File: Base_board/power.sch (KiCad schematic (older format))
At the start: 39 parts, among them J13 Wire pad, J14 Wire pad, J15 Wire pad, J16 Wire pad, J9 USB_A, Q6 2N7002, SW3 SW_Push, U3 MCP16331T-E/CH, U4 BTS50080-1TEA, U5 DC_DC_POL

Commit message: Fix older symbols assignation
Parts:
- C10, C26, C4, C5, C7, C8, C9: symbol KXKM_audio_battery_module-rescue:C_Small -> Device:C_Small
- C6: symbol KXKM_audio_battery_module-rescue:CP1_Small -> Device:CP1_Small
- D13, D2: symbol KXKM_audio_battery_module-rescue:D_Zener_Small -> Device:D_Zener_Small
- D3: symbol KXKM_audio_battery_module-rescue:D_Schottky_Small -> Device:D_Schottky_Small
- L1: symbol KXKM_audio_battery_module-rescue:L_Small -> Device:L_Small
- R1, R10, R12, R22, R8, R9: symbol KXKM_audio_battery_module-rescue:R_Small -> Device:R_Small
- SW3: symbol KXKM_audio_battery_module-rescue:SW_Push -> Switch:SW_Push
- U3: symbol KXKM_audio_battery_module-rescue:MCP16301H -> Regulator_Switching:MCP16331CH
- U5: symbol KXKM_audio_battery_module-rescue:DC_DC_POL -> tom_kicad:DC_DC_POL
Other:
- moved on the sheet: U3
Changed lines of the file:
@@
 EESchema Schematic File Version 4
-LIBS:KXKM_audio_battery_module-cache
+LIBS:KXKM_ESP32_battery_management_board-cache
 EELAYER 29 0
 EELAYER END
@@
 Battery power output.\nMax 10A
 $Comp
-L KXKM_audio_battery_module-rescue:DC_DC_POL U5
+L tom_kicad:DC_DC_POL U5
 U 1 1 5A9FAEA4
 P 8650 2350
@@
 Optional 3A  buck module \nwith USB connector
 $Comp
-L KXKM_audio_battery_module-rescue:SW_Push SW3
+L Switch:SW_Push SW3
 U 1 1 5A9FC5E1
 P 3150 4900
@@
 $EndComp
 $Comp
-L KXKM_audio_battery_module-rescue:GND #PWR035
+L power:GND #PWR035
 U 1 1 5A9FC90F
 P 2150 1700
@@
 MAIN_OUT_EN
 $Comp
-L KXKM_audio_battery_module-rescue:C_Small C5
+L Device:C_Small C5
 U 1 1 5A9FED2B
 P 2000 6800
@@
 $EndComp
 $Comp
-L KXKM_audio_battery_module-rescue:C_Small C4
+L Device:C_Small C4
 U 1 1 5A9FEE3B
 P 1600 6800
@@
 $EndComp
 $Comp
-L KXKM_audio_battery_module-rescue:+BATT #PWR037
+L power:+BATT #PWR037
 U 1 1 5A9FF065
 P 2800 1250
@@
 $EndComp
 $Comp
-L KXKM_audio_battery_module-rescue:GND #PWR038
+L power:GND #PWR038
 U 1 1 5A9FF120
 P 1600 6900
@@
 $EndComp
 $Comp
-L KXKM_audio_battery_module-rescue:GND #PWR039
+L power:GND #PWR039
 U 1 1 5A9FF156
 P 2000 6900
@@
 $EndComp
 $Comp
-L KXKM_audio_battery_module-rescue:C_Small C7
+L Device:C_Small C7
 U 1 1 5A9FF342
 P 3800 6600
@@
 $EndComp
 $Comp
-L KXKM_audio_battery_module-rescue:D_Schottky_Small D3
+L Device:D_Schottky_Small D3
 U 1 1 5A9FF573
 P 3800 6850
@@
 $EndComp
 $Comp
-L KXKM_audio_battery_module-rescue:GND #PWR040
+L power:GND #PWR040
 U 1 1 5A9FF8A5
-P 3250 7350
-F 0 "#PWR040" H 3250 7100 50  0001 C CNN
-F 1 "GND" H 3250 7200 50  0000 C CNN
-F 2 "" H 3250 7350 50  0001 C CNN
-F 3 "" H 3250 7350 50  0001 C CNN
-	1    3250 7350
-	1    0    0    -1
-$EndComp
-$Comp
-L KXKM_audio_battery_module-rescue:GND #PWR041
+P 3250 7050
+F 0 "#PWR040" H 3250 6800 50  0001 C CNN
+F 1 "GND" H 3250 6900 50  0000 C CNN
+F 2 "" H 3250 7050 50  0001 C CNN
+F 3 "" H 3250 7050 50  0001 C CNN
+	1    3250 7050
+	1    0    0    -1
+$EndComp
+$Comp
+L power:GND #PWR041
 U 1 1 5A9FF8DA
 P 3800 6950
@@
 $EndComp
 $Comp
-L KXKM_audio_battery_module-rescue:MCP16301H U3
+L Regulator_Switching:MCP16331CH U3
 U 1 1 5A9FC3B6
-P 3250 6950
-F 0 "U3" H 2950 7500 50  0000 L CNN
-F 1 "MCP16331T-E/CH" H 2950 7400 50  0000 L CNN
-F 2 "Package_TO_SOT_SMD:SOT-23-6" H 3250 6450 50  0001 C CNN
-F 3 "" H 2950 7500 50  0001 C CNN
-	1    3250 6950
-	1    0    0    -1
-$EndComp
-$Comp
-L KXKM_audio_battery_module-rescue:L_Small L1
+P 3250 6750
+F 0 "U3" H 3200 7100 50  0000 L CNN
+F 1 "MCP16331T-E/CH" H 2900 7000 50  0000 L CNN
+F 2 "Package_TO_SOT_SMD:SOT-23-6" H 3250 6250 50  0001 C CNN
+F 3 "" H 2950 7300 50  0001 C CNN
+	1    3250 6750
+	1    0    0    -1
+$EndComp
+$Comp
+L Device:L_Small L1
 U 1 1 5A9FFE27
 P 4300 6750
@@
 $EndComp
 $Comp
-L KXKM_audio_battery_module-rescue:R_Small R9
+L Device:R_Small R9
 U 1 1 5AA004D5
 P 4600 6950
@@
 $EndComp
 $Comp
-L KXKM_audio_battery_module-rescue:R_Small R10
+L Device:R_Small R10
 U 1 1 5AA0053D
 P 4600 7300
@@
 $EndComp
 $Comp
-L KXKM_audio_battery_module-rescue:GND #PWR042
+L power:GND #PWR042
 U 1 1 5AA00713
 P 4600 7450
@@
 $EndComp
 $Comp
-L KXKM_audio_battery_module-rescue:C_Small C8
+L Device:C_Small C8
 U 1 1 5AA00938
 P 5100 6950
@@
 $EndComp
 $Comp
-L KXKM_audio_battery_module-rescue:C_Small C9
+L Device:C_Small C9
 U 1 1 5AA00C46
 P 5500 6950
@@
 $EndComp
 $Comp
-L KXKM_audio_battery_module-rescue:C_Small C10
+L Device:C_Small C10
 U 1 1 5AA00D4C
 P 5950 6950
@@
 $EndComp
 $Comp
-L KXKM_audio_battery_module-rescue:GND #PWR043
+L power:GND #PWR043
 U 1 1 5AA00DA9
 P 5500 7050
@@
 $EndComp
 $Comp
-L KXKM_audio_battery_module-rescue:GND #PWR044
+L power:GND #PWR044
 U 1 1 5AA00DF3
 P 5950 7050
@@
 $EndComp
 $Comp
-L KXKM_audio_battery_module-rescue:+3.3V #PWR045
+L power:+3.3V #PWR045
 U 1 1 5AA00ECC
 P 5950 6700
@@
 3.3V_EN
 $Comp
-L KXKM_audio_battery_module-rescue:D_Zener_Small D2
+L Device:D_Zener_Small D2
 U 1 1 5AA028CA
 P 3150 5600
@@
 $EndComp
 $Comp
-L KXKM_audio_battery_module-rescue:R_Small R8
+L Device:R_Small R8
 U 1 1 5AA0358A
 P 3150 5250
@@
 $EndComp
 $Comp
-L KXKM_audio_battery_module-rescue:GND #PWR047
+L power:GND #PWR047
 U 1 1 5AA037A6
 P 3150 5700
@@
 The MCP16331 has an internal pull up on the EN pin.\n\nOn startup, R1 pulls EN low (system Off)\n\nWhen the push button is pressed, the Zener is powered and \nthe EN pin gets high through D1 => system On.\n\nThe uC gets powered and can now controls the system state \nwith the 3.3V_EN line.\nIt can also monitor future states of the push button.
 $Comp
-L KXKM_audio_battery_module-rescue:VBUS #PWR048
+L power:VBUS #PWR048
 U 1 1 5AA2DF17
 P 9400 2200
@@
 $EndComp
 $Comp
-L KXKM_audio_battery_module-rescue:CP1_Small C6
+L Device:CP1_Small C6
 U 1 1 5AA2FD90
 P 2150 1500
@@
 $EndComp
 $Comp
-L KXKM_audio_battery_module-rescue:GND #PWR051
+L power:GND #PWR051
 U 1 1 5AA32CAF
 P 9400 1650
@@
 $EndComp
 $Comp
-L KXKM_audio_battery_module-rescue:GND #PWR052
+L power:GND #PWR052
 U 1 1 5AA32D09
 P 9400 2600
@@
 10A high side load switch
 $Comp
-L KXKM_audio_battery_module-rescue:GND #PWR053
+L power:GND #PWR053
 U 1 1 5AA356E4
 P 5150 1800
@@
 $EndComp
 $Comp
-L KXKM_audio_battery_module-rescue:GND #PWR054
+L power:GND #PWR054
 U 1 1 5AA35B5B
 P 4800 1800
@@
 $EndComp
 $Comp
-L KXKM_audio_battery_module-rescue:R_Small R12
+L Device:R_Small R12
 U 1 1 5AA35ECE
 P 6800 2150
@@
 $EndComp
 $Comp
-L KXKM_audio_battery_module-rescue:GND #PWR055
+L power:GND #PWR055
 U 1 1 5AA35FB7
 P 6800 2500
@@
 LOAD_I_SENSE
 $Comp
-L KXKM_audio_battery_module-rescue:PWR_FLAG #FLG057
+L power:PWR_FLAG #FLG057
 U 1 1 5AA444FE
 P 6300 6700
@@
 R8 selection :\nZener current : 5mA min, 100mA max \n470R : \n    5mA with VBat = 5.5V\n    57mA with VBat = 30V
 $Comp
-L KXKM_audio_battery_module-rescue:+VSW #PWR062
+L power:+VSW #PWR062
 U 1 1 5AA7A913
 P 7900 1300
@@
 	2000 6650 2000 6700
 Wire Wire Line
-	3650 6950 3700 6950
-Wire Wire Line
-	3700 6950 3700 7150
-Wire Wire Line
 	3700 7150 4600 7150
 Wire Wire Line
@@
 	9300 2400 9400 2400
 $Comp
-L KXKM_audio_battery_module-rescue:R_Small R1
+L Device:R_Small R1
 U 1 1 5AAAA24E
 P 2500 6950
@@
 $EndComp
 $Comp
-L KXKM_audio_battery_module-rescue:GND #PWR063
+L power:GND #PWR063
 U 1 1 5AAAA2EA
 P 2500 7050
@@
 	2800 1350 2800 1400
 $Comp
-L KXKM_audio_battery_module-rescue:GND #PWR0101
+L power:GND #PWR0101
 U 1 1 5C6E6168
 P 2800 1700
@@
 Connection ~ 2800 1350
 $Comp
-L KXKM_audio_battery_module-rescue:C_Small C26
+L Device:C_Small C26
 U 1 1 5C712B7A
 P 2650 6950
@@
 $EndComp
 $Comp
-L KXKM_audio_battery_module-rescue:GND #PWR0106
+L power:GND #PWR0106
 U 1 1 5C717150
 P 2650 7050
@@
 R_IS selection : I_IS = 6mA max\nIn normal conditions, I_IS = I_load / 10000\n=> with R_IS = 2k, I_load = 10A gives 2V. \nThe Zener clamps voltage to 3V (error conditions => I_IS = 5.2mA)
 $Comp
-L KXKM_audio_battery_module-rescue:D_Zener_Small D13
+L Device:D_Zener_Small D13
 U 1 1 5C7A51DB
 P 7050 2150
@@
 	7050 1900 7100 1900
 $Comp
-L KXKM_audio_battery_module-rescue:GND #PWR0107
+L power:GND #PWR0107
 U 1 1 5C7A9F58
 P 7050 2250
@@
 $EndComp
 $Comp
-L KXKM_audio_battery_module-rescue:R_Small R22
+L Device:R_Small R22
 U 1 1 5C7B3CFC
 P 6800 2350
@@
 $EndComp
 $Comp
-L KXKM_audio_battery_module-rescue:GND #PWR0102
+L power:GND #PWR0102
 U 1 1 5C7F26AF
 P 9800 4400
@@
 $EndComp
 $Comp
-L KXKM_audio_battery_module-rescue:GND #PWR0105
+L power:GND #PWR0105
 U 1 1 5C7F2704
 P 9900 4400
@@
 	1900 1650 2150 1650
 $Comp
-L KXKM_audio_battery_module-rescue:+BATT #PWR046
+L power:+BATT #PWR046
 U 1 1 5AA027F2
 P 3150 4600
@@
 	6200 900  6350 900
 $Comp
-L KXKM_audio_battery_module-rescue:+BATT #PWR0108
+L power:+BATT #PWR0108
 U 1 1 5CD9FDB2
 P 1600 6600
@@
 	2150 950  2100 950
 $Comp
-L KXKM_audio_battery_module-rescue:PWR_FLAG #FLG0101
+L power:PWR_FLAG #FLG0101
 U 1 1 5CDEEF8F
 P 2150 900
@@
 	5950 1500 5950 1900
 $Comp
-L KXKM_audio_battery_module-rescue:+BATT #PWR061
+L power:+BATT #PWR061
 U 1 1 5AA46EC2
 P 10350 6200
@@
 $EndComp
 $Comp
-L KXKM_audio_battery_module-rescue:PWR_FLAG #FLG060
+L power:PWR_FLAG #FLG060
 U 1 1 5AA46E7F
 P 10350 6200
@@
 For most newer devices, a 0R resistor between D+ and D-\nshould be enough to indicate that the port can supply up to 1.5A.\n\nOlder Apple devices may need specific voltage dividers \non D+/D- lines.\nCheck https://lygte-info.dk/info/USBinfo%20UK.html
 $Comp
-L KXKM_audio_battery_module-rescue:VBUS #PWR027
+L power:VBUS #PWR027
 U 1 1 5CBCF1C7
 P 9400 3700
@@
 $EndComp
 $Comp
-L KXKM_audio_battery_module-rescue:VBUS #PWR025
+L power:VBUS #PWR025
 U 1 1 5CBD526E
 P 8850 3650
@@
 $EndComp
 $Comp
-L KXKM_audio_battery_module-rescue:VBUS #PWR023
+L power:VBUS #PWR023
 U 1 1 5CBD54F6
 P 8500 3650
@@
 $EndComp
 $Comp
-L KXKM_audio_battery_module-rescue:GND #PWR026
+L power:GND #PWR026
 U 1 1 5CBD5908
 P 8850 4450
@@
 $EndComp
 $Comp
-L KXKM_audio_battery_module-rescue:GND #PWR024
+L power:GND #PWR024
 U 1 1 5CBD5C75
 P 8500 4450
@@
 	9400 4100 9400 4200
 Connection ~ 9300 4200
+Wire Wire Line
+	3650 6850 3700 6850
+Wire Wire Line
+	3700 6850 3700 7150
 $EndSCHEMATC

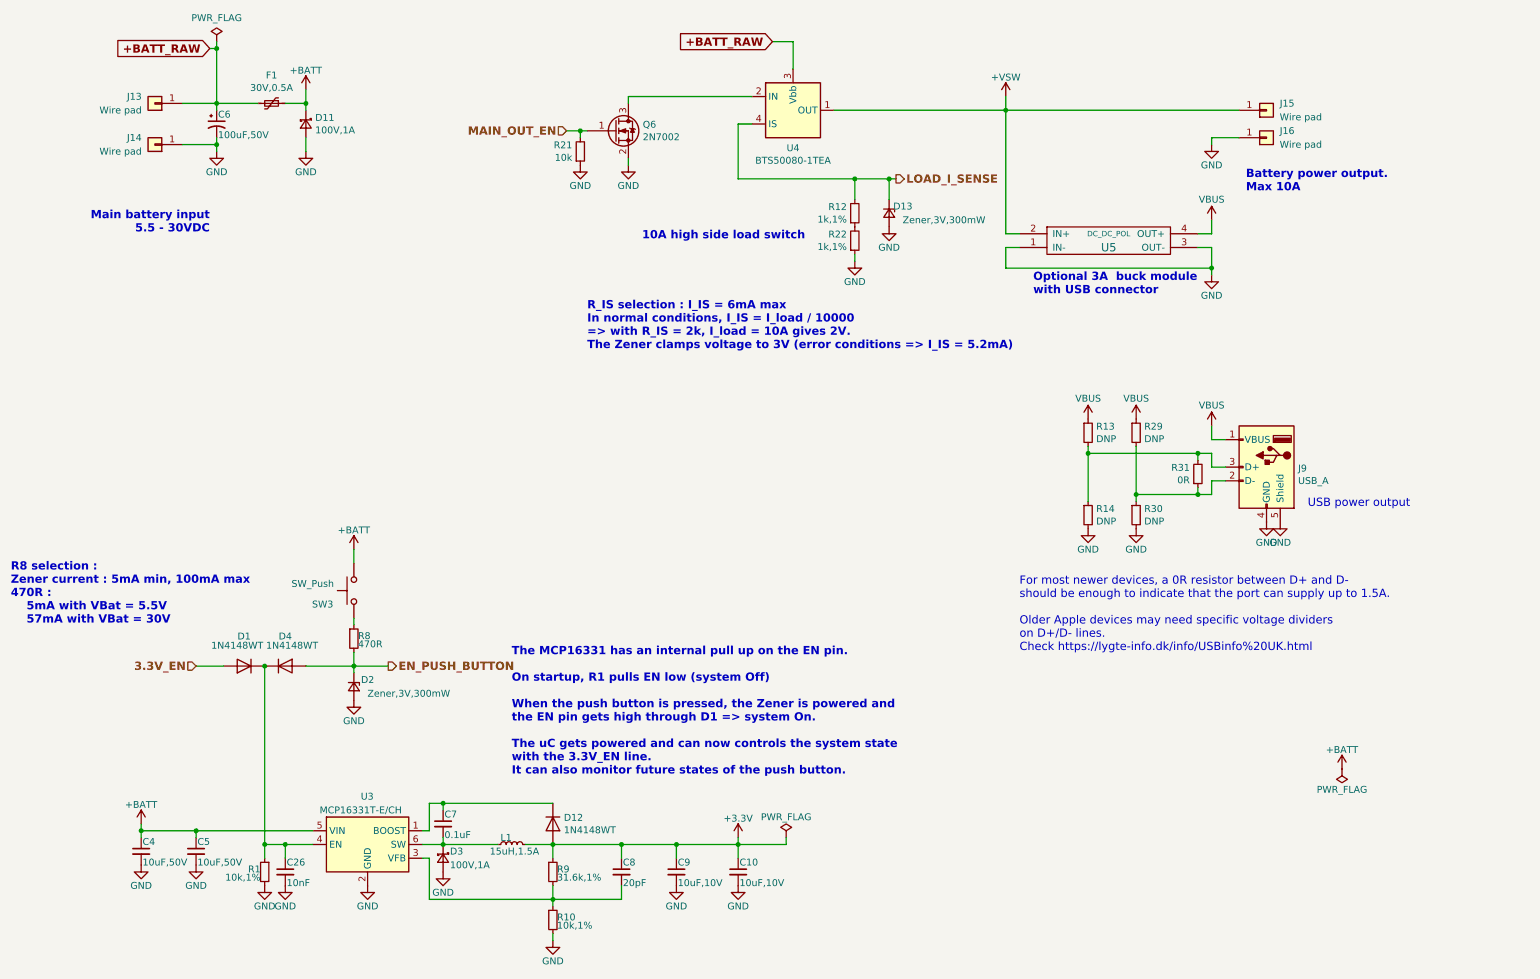
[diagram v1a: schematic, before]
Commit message: Fix component values > pick n place convention
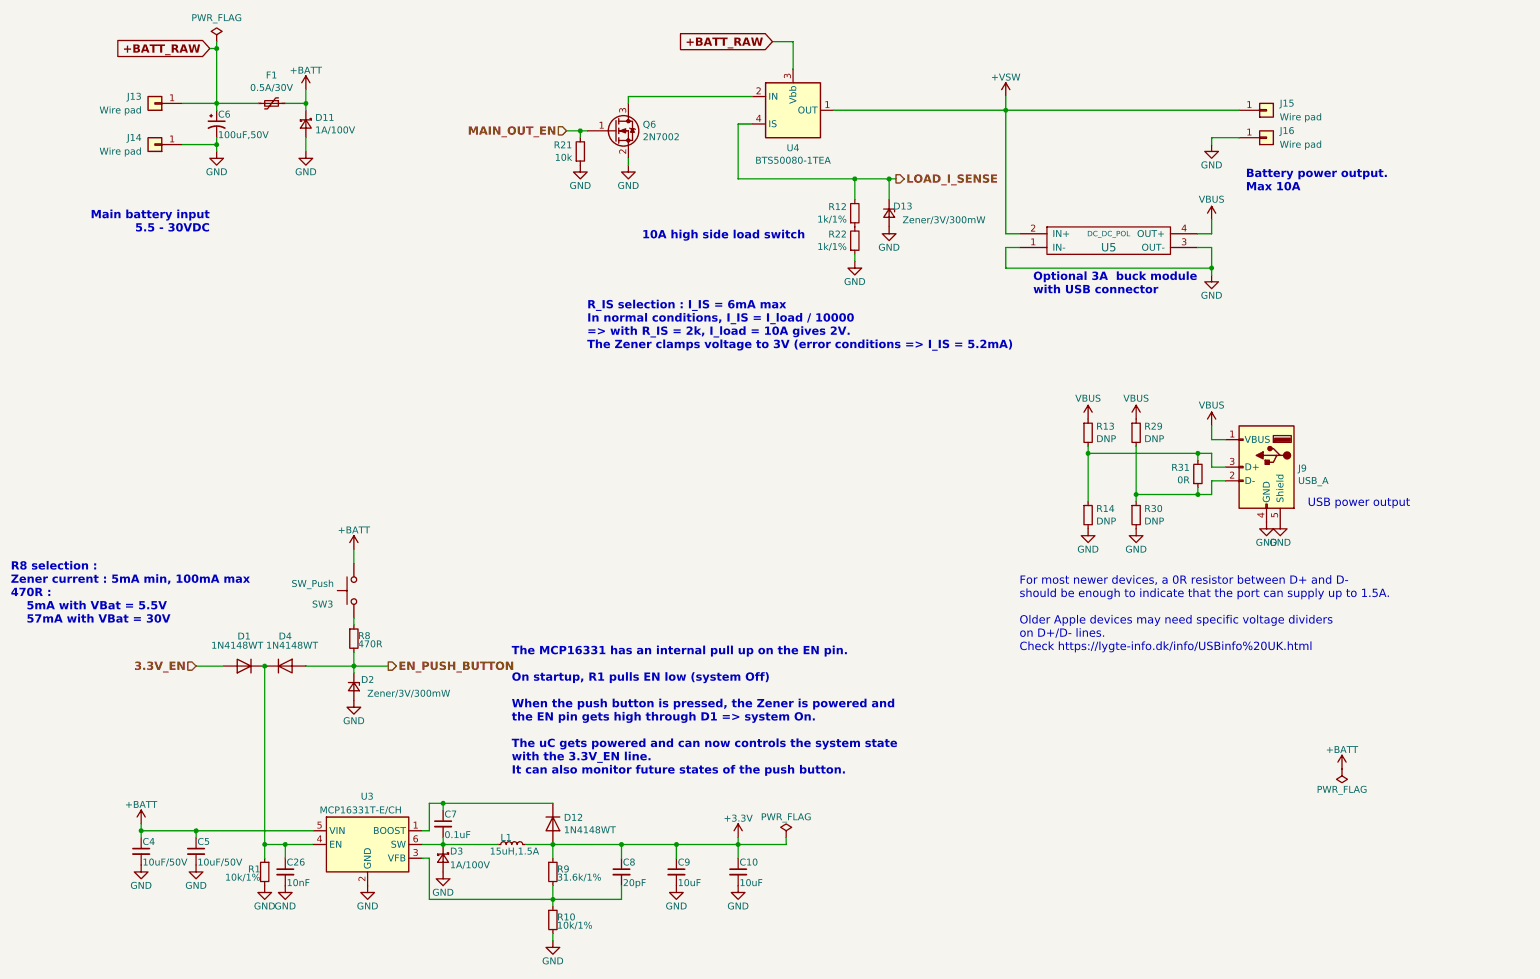
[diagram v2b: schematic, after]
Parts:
- C10, C9: value 10uF,10V -> 10uF
- C4, C5: value 10uF,50V -> 10uF/50V
- D11, D3: value 100V,1A -> 1A/100V
- D13, D2: value Zener,3V,300mW -> Zener/3V/300mW
- F1: value 30V,0.5A -> 0.5A/30V
- R1, R10: value 10k,1% -> 10k/1%
- R12, R22: value 1k,1% -> 1k/1%
- R9: value 31.6k,1% -> 31.6k/1%
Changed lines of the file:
@@
 P 2000 6800
 F 0 "C5" H 2010 6870 50  0000 L CNN
-F 1 "10uF,50V" H 2010 6720 50  0000 L CNN
+F 1 "10uF/50V" H 2010 6720 50  0000 L CNN
 F 2 "Capacitor_SMD:C_1206_3216Metric" H 2000 6800 50  0001 C CNN
 F 3 "" H 2000 6800 50  0001 C CNN
@@
 P 1600 6800
 F 0 "C4" H 1610 6870 50  0000 L CNN
-F 1 "10uF,50V" H 1610 6720 50  0000 L CNN
+F 1 "10uF/50V" H 1610 6720 50  0000 L CNN
 F 2 "Capacitor_SMD:C_1206_3216Metric" H 1600 6800 50  0001 C CNN
 F 3 "" H 1600 6800 50  0001 C CNN
@@
 P 3800 6850
 F 0 "D3" V 3750 6900 50  0000 L CNN
-F 1 "100V,1A" V 3850 6900 50  0000 L CNN
+F 1 "1A/100V" V 3850 6900 50  0000 L CNN
 F 2 "Diode_SMD:D_SMA" V 3800 6850 50  0001 C CNN
 F 3 "" V 3800 6850 50  0001 C CNN
@@
 P 4600 6950
 F 0 "R9" H 4630 6970 50  0000 L CNN
-F 1 "31.6k,1%" H 4630 6910 50  0000 L CNN
+F 1 "31.6k/1%" H 4630 6910 50  0000 L CNN
 F 2 "Resistor_SMD:R_0603_1608Metric" H 4600 6950 50  0001 C CNN
 F 3 "" H 4600 6950 50  0001 C CNN
@@
 P 4600 7300
 F 0 "R10" H 4630 7320 50  0000 L CNN
-F 1 "10k,1%" H 4630 7260 50  0000 L CNN
+F 1 "10k/1%" H 4630 7260 50  0000 L CNN
 F 2 "Resistor_SMD:R_0603_1608Metric" H 4600 7300 50  0001 C CNN
 F 3 "" H 4600 7300 50  0001 C CNN
@@
 P 5500 6950
 F 0 "C9" H 5510 7020 50  0000 L CNN
-F 1 "10uF,10V" H 5510 6870 50  0000 L CNN
+F 1 "10uF" H 5510 6870 50  0000 L CNN
 F 2 "Capacitor_SMD:C_0805_2012Metric" H 5500 6950 50  0001 C CNN
 F 3 "" H 5500 6950 50  0001 C CNN
@@
 P 5950 6950
 F 0 "C10" H 5960 7020 50  0000 L CNN
-F 1 "10uF,10V" H 5960 6870 50  0000 L CNN
+F 1 "10uF" H 5960 6870 50  0000 L CNN
 F 2 "Capacitor_SMD:C_0805_2012Metric" H 5950 6950 50  0001 C CNN
 F 3 "" H 5950 6950 50  0001 C CNN
@@
 P 3150 5600
 F 0 "D2" V 3100 5700 50  0000 C CNN
-F 1 "Zener,3V,300mW" V 3200 6000 50  0000 C CNN
+F 1 "Zener/3V/300mW" V 3200 6000 50  0000 C CNN
 F 2 "Diode_SMD:D_SOD-323" V 3150 5600 50  0001 C CNN
 F 3 "" V 3150 5600 50  0001 C CNN
@@
 P 6800 2150
 F 0 "R12" H 6742 2104 50  0000 R CNN
-F 1 "1k,1%" H 6742 2195 50  0000 R CNN
+F 1 "1k/1%" H 6742 2195 50  0000 R CNN
 F 2 "Resistor_SMD:R_0603_1608Metric" H 6800 2150 50  0001 C CNN
 F 3 "" H 6800 2150 50  0001 C CNN
@@
 P 2500 6950
 F 0 "R1" H 2530 6970 50  0000 L CNN
-F 1 "10k,1%" H 2530 6910 50  0000 L CNN
+F 1 "10k/1%" H 2530 6910 50  0000 L CNN
 F 2 "Resistor_SMD:R_0603_1608Metric" H 2500 6950 50  0001 C CNN
 F 3 "" H 2500 6950 50  0001 C CNN
@@
 P 2550 1350
 F 0 "F1" V 2345 1350 50  0000 C CNN
-F 1 "30V,0.5A" V 2436 1350 50  0000 C CNN
+F 1 "0.5A/30V" V 2436 1350 50  0000 C CNN
 F 2 "Fuse:Fuse_1812_4532Metric" H 2600 1150 50  0001 L CNN
 F 3 "~" H 2550 1350 50  0001 C CNN
@@
 P 2800 1500
 F 0 "D11" V 2754 1568 50  0000 L CNN
-F 1 "100V,1A" V 2845 1568 50  0000 L CNN
+F 1 "1A/100V" V 2845 1568 50  0000 L CNN
 F 2 "Diode_SMD:D_SMA" V 2800 1500 50  0001 C CNN
 F 3 "~" V 2800 1500 50  0001 C CNN
@@
 P 7050 2150
 F 0 "D13" V 7000 2250 50  0000 C CNN
-F 1 "Zener,3V,300mW" V 7100 2550 50  0000 C CNN
+F 1 "Zener/3V/300mW" V 7100 2550 50  0000 C CNN
 F 2 "Diode_SMD:D_SOD-323" V 7050 2150 50  0001 C CNN
 F 3 "" V 7050 2150 50  0001 C CNN
@@
 P 6800 2350
 F 0 "R22" H 6742 2304 50  0000 R CNN
-F 1 "1k,1%" H 6742 2395 50  0000 R CNN
+F 1 "1k/1%" H 6742 2395 50  0000 R CNN
 F 2 "Resistor_SMD:R_0603_1608Metric" H 6800 2350 50  0001 C CNN
 F 3 "" H 6800 2350 50  0001 C CNN
